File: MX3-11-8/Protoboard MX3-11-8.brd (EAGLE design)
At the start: 74.4 x 99.4 mm, 120 parts, among them J1 DCJ0202, U1 3.3V/150mA

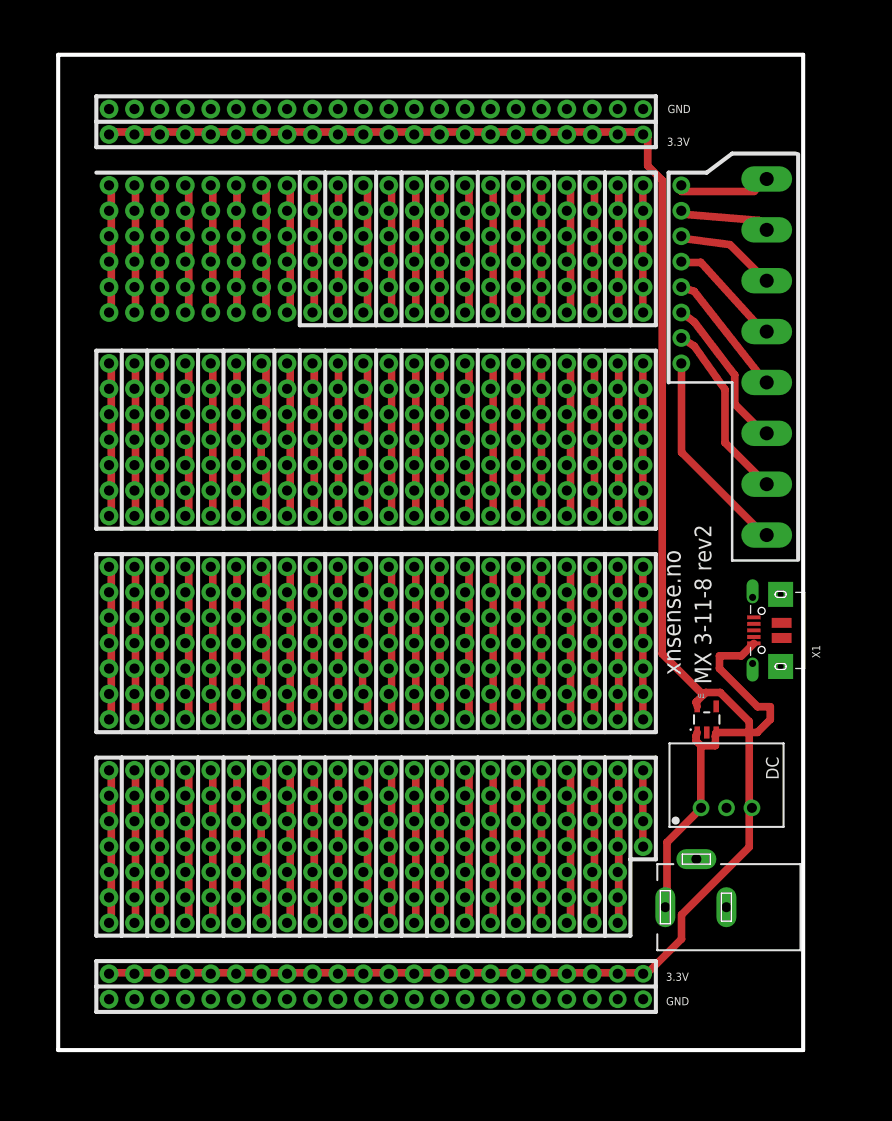
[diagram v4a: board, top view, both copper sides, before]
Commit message: Routed and Gerb files
Routed and produced gerb files
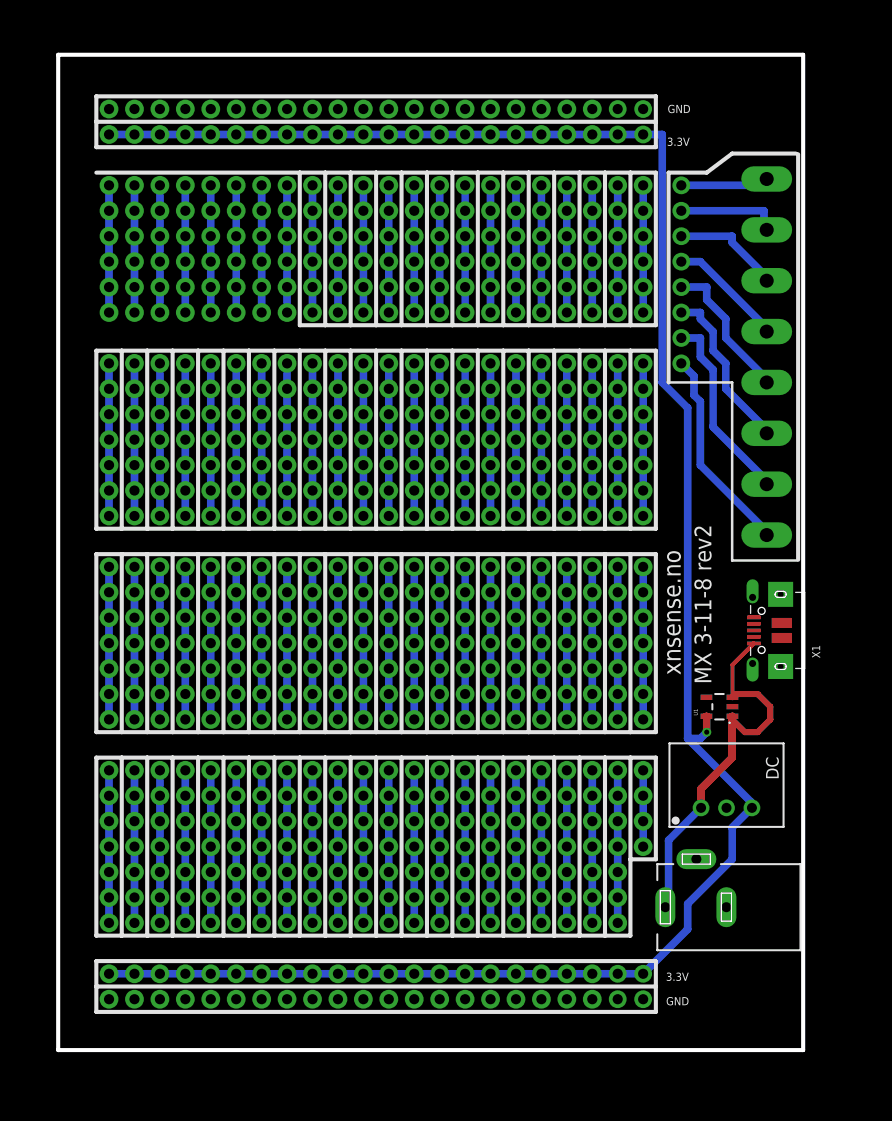
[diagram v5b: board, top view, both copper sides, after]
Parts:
- moved U1 1.80 mm to (66.0, 34.3), turned to 90 degrees
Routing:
- net VDD: track 209.2 -> 204.4 mm, vias 0 -> 1
- net N$29: track 18.1 -> 15.2 mm
- net N$51: track 18.1 -> 15.2 mm
- net N$37: track 18.1 -> 15.2 mm
- net N$59: track 18.1 -> 15.2 mm
- net N$77: track 18.0 -> 15.2 mm
- net N$33: track 17.9 -> 15.2 mm
- net N$55: track 17.9 -> 15.2 mm
- net N$7: track 15.3 -> 12.7 mm
- net N$73: track 17.8 -> 15.2 mm
- net N$63: track 17.8 -> 15.2 mm
- net N$41: track 17.8 -> 15.2 mm
- net N$81: track 17.8 -> 15.2 mm
- net N$11: track 15.1 -> 12.7 mm
- net N$48: track 17.5 -> 15.2 mm
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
